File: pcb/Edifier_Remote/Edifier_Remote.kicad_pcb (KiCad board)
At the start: 2 copper layers, 33 x 70 mm, 9 parts, among them Q1 Q_NPN_BCE

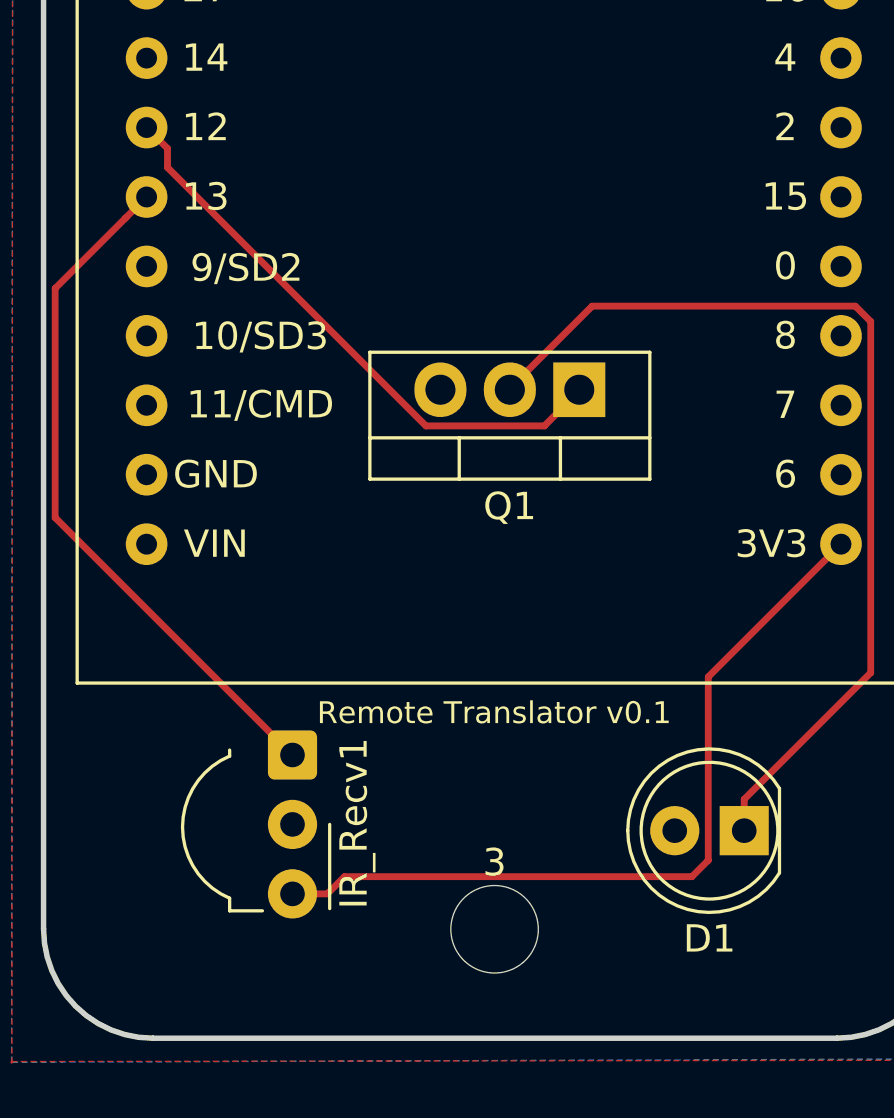
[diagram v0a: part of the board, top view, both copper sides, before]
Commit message: add some labels and rotate Q1
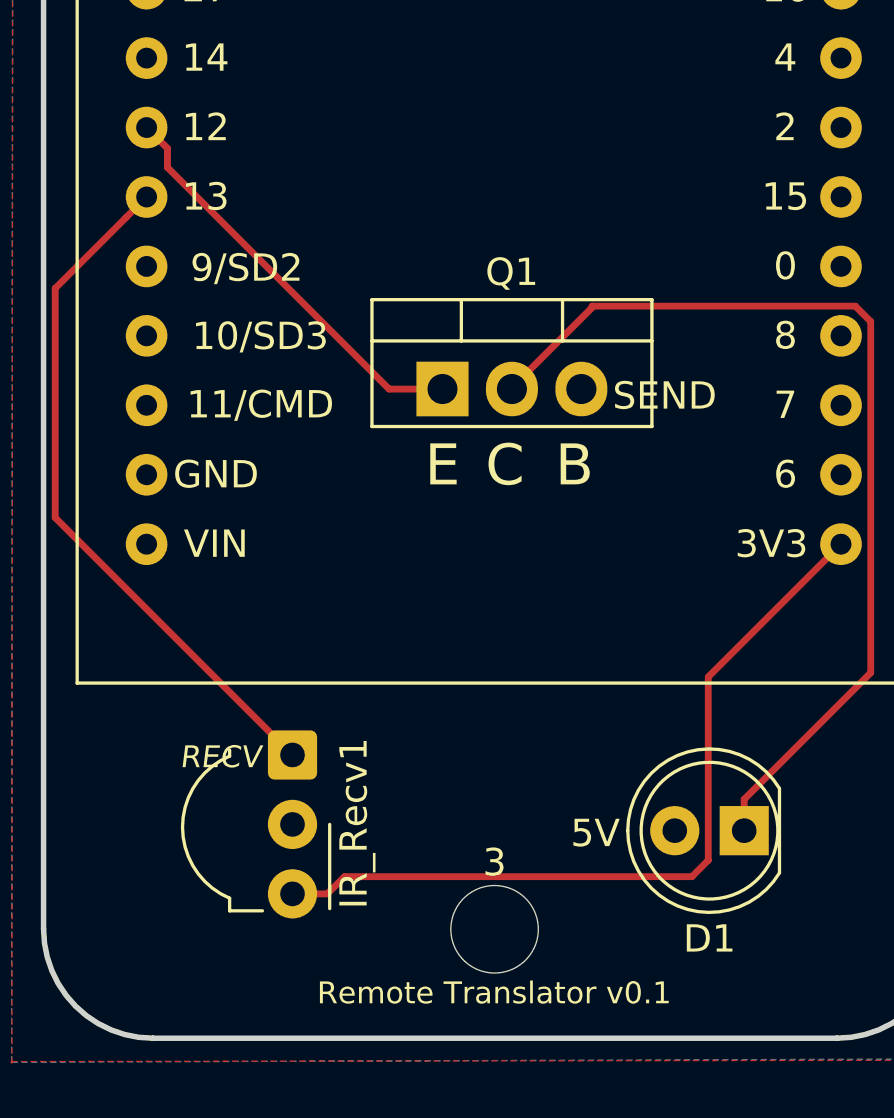
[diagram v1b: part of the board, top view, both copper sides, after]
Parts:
- moved Q1 5.00 mm to (115.6, 112.5), turned to 0 degrees
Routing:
- net /SEND: track 21.3 -> 15.2 mm
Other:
- board text added: "5V"
- board text added: "B"
- board text added: "C"
- board text added: "E"
- board text added: "RECV"
- board text added: "SEND"
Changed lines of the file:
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@@
-(kicad_pcb (version 20171130) (host pcbnew "(5.1.2)-2")
+(kicad_pcb (version 20171130) (host pcbnew 5.0.2)
   (general
     (thickness 1.6)
-    (drawings 3)
-    (tracks 23)
+    (drawings 9)
+    (tracks 24)
     (zones 0)
     (modules 9)
@@
     (zone_45_only no)
     (trace_min 0.2)
+    (segment_width 0.2)
+    (edge_width 0.1)
     (via_size 0.8)
     (via_drill 0.4)
@@
     (uvia_min_size 0.2)
     (uvia_min_drill 0.1)
-    (edge_width 0.1)
-    (segment_width 0.2)
     (pcb_text_width 0.3)
     (pcb_text_size 1.5 1.5)
@@
     (pad_drill 0.762)
     (pad_to_mask_clearance 0)
+    (solder_mask_min_width 0.25)
     (aux_axis_origin 0 0)
     (visible_elements 7FFFFFFF)
@@
       (outputformat 1)
       (mirror false)
-      (drillshape 1)
+      (drillshape 0)
       (scaleselection 1)
-      (outputdirectory ""))
+      (outputdirectory "../Gerber/"))
   )
   (net 0 "")
@@
   )
   (module Package_TO_SOT_THT:TO-220-3_Vertical (layer F.Cu)
-    (at 120.5738 112.5474 180)
+    (at 115.57 112.522)
     (descr "TO-220-3, Vertical, RM 2.54mm, see https://www.vishay.com/docs/66542/to-220-1.pdf")
     (tags "TO-220-3 Vertical RM 2.54mm")
-    (fp_text reference Q1 (at 2.54 -4.27) (layer F.SilkS)
-      (effects (font (size 1 1) (thickness 0.15)))
-    )
-    (fp_text value Q_NPN_BCE (at 2.54 2.5) (layer F.Fab)
-      (effects (font (size 1 1) (thickness 0.15)))
-    )
-    (fp_text user %R (at 2.54 -4.27) (layer F.Fab)
+    (fp_text reference Q1 (at 2.54 -4.27 -180) (layer F.SilkS)
+      (effects (font (size 1 1) (thickness 0.15)))
+    )
+    (fp_text value Q_NPN_BCE (at 1.9558 -2.5146 -180) (layer F.Fab)
+      (effects (font (size 1 1) (thickness 0.15)))
+    )
+    (fp_text user %R (at 2.54 -4.27 -180) (layer F.Fab)
       (effects (font (size 1 1) (thickness 0.15)))
     )
@@
     (fp_line (start -2.46 1.25) (end 7.54 1.25) (layer F.Fab) (width 0.1))
     (fp_line (start -2.46 -3.15) (end -2.46 1.25) (layer F.Fab) (width 0.1))
-    (pad 3 thru_hole oval (at 5.08 0 180) (size 1.905 2) (drill 1.1) (layers *.Cu *.Mask)
+    (pad 3 thru_hole oval (at 5.08 0) (size 1.905 2) (drill 1.1) (layers *.Cu *.Mask)
       (net 4 GND))
-    (pad 2 thru_hole oval (at 2.54 0 180) (size 1.905 2) (drill 1.1) (layers *.Cu *.Mask)
+    (pad 2 thru_hole oval (at 2.54 0) (size 1.905 2) (drill 1.1) (layers *.Cu *.Mask)
       (net 2 "Net-(D1-Pad1)"))
-    (pad 1 thru_hole rect (at 0 0 180) (size 1.905 2) (drill 1.1) (layers *.Cu *.Mask)
+    (pad 1 thru_hole rect (at 0 0) (size 1.905 2) (drill 1.1) (layers *.Cu *.Mask)
       (net 6 /SEND))
     (model ${KISYS3DMOD}/Package_TO_SOT_THT.3dshapes/TO-220-3_Vertical.wrl
@@
     )
   )
+  (gr_text E (at 115.57 115.316) (layer F.SilkS)
+    (effects (font (size 1.5 1.5) (thickness 0.3)))
+  )
+  (gr_text C (at 117.856 115.316) (layer F.SilkS)
+    (effects (font (size 1.5 1.5) (thickness 0.3)))
+  )
+  (gr_text B (at 120.396 115.316) (layer F.SilkS)
+    (effects (font (size 1.5 1.5) (thickness 0.3)))
+  )
+  (gr_text SEND (at 123.698 112.776) (layer F.SilkS)
+    (effects (font (size 1 1) (thickness 0.25)))
+  )
+  (gr_text RECV (at 107.442 125.984) (layer F.SilkS)
+    (effects (font (size 0.8 0.8) (thickness 0.2) italic))
+  )
+  (gr_text 5V (at 121.158 128.778) (layer F.SilkS)
+    (effects (font (size 1 1) (thickness 0.25)))
+  )
   (gr_text "Remote Translator v0.1" (at 117.6782 89.5096) (layer B.SilkS)
     (effects (font (size 1 1) (thickness 0.15)) (justify mirror))
@@
     (effects (font (size 1 1) (thickness 0.15)) (justify mirror))
   )
-  (gr_text "Remote Translator v0.1\n" (at 117.4623 124.3711) (layer F.SilkS)
+  (gr_text "Remote Translator v0.1\n" (at 117.4623 134.62) (layer F.SilkS)
     (effects (font (size 0.8 0.8) (thickness 0.15)))
   )
-  (segment (start 118.0338 112.4999) (end 118.0338 112.5474) (width 0.25) (layer F.Cu) (net 2))
-  (segment (start 121.043701 109.489999) (end 118.0338 112.4999) (width 0.25) (layer F.Cu) (net 2))
   (segment (start 131.234001 110.055239) (end 130.668761 109.489999) (width 0.25) (layer F.Cu) (net 2))
   (segment (start 131.234001 122.898699) (end 131.234001 110.055239) (width 0.25) (layer F.Cu) (net 2))
@@
   (segment (start 126.6063 127.5264) (end 131.234001 122.898699) (width 0.25) (layer F.Cu) (net 2))
   (segment (start 126.6063 128.6764) (end 126.6063 127.5264) (width 0.25) (layer F.Cu) (net 2))
+  (segment (start 118.0338 112.4999) (end 118.0338 112.5474) (width 0.25) (layer F.Cu) (net 2))
+  (segment (start 118.11 112.4745) (end 118.11 112.522) (width 0.25) (layer F.Cu) (net 2))
+  (segment (start 121.043701 109.540799) (end 118.11 112.4745) (width 0.25) (layer F.Cu) (net 2))
+  (segment (start 121.043701 109.489999) (end 121.043701 109.540799) (width 0.25) (layer F.Cu) (net 2))
   (segment (start 111.985993 130.358199) (end 124.693999 130.358199) (width 0.25) (layer F.Cu) (net 3))
   (segment (start 110.0836 130.9878) (end 111.356392 130.9878) (width 0.25) (layer F.Cu) (net 3))
@@
   (segment (start 105.508999 103.718999) (end 104.747 102.957) (width 0.25) (layer F.Cu) (net 6))
   (segment (start 105.508999 104.41677) (end 105.508999 103.718999) (width 0.25) (layer F.Cu) (net 6))
-  (segment (start 114.964639 113.87241) (end 105.508999 104.41677) (width 0.25) (layer F.Cu) (net 6))
-  (segment (start 119.29629 113.87241) (end 114.964639 113.87241) (width 0.25) (layer F.Cu) (net 6))
-  (segment (start 120.5738 112.5949) (end 119.29629 113.87241) (width 0.25) (layer F.Cu) (net 6))
-  (segment (start 120.5738 112.5474) (end 120.5738 112.5949) (width 0.25) (layer F.Cu) (net 6))
+  (segment (start 120.5738 112.5474) (end 120.5738 112.5949) (width 0.25) (layer F.Cu) (net 4))
+  (segment (start 113.614229 112.522) (end 115.57 112.522) (width 0.25) (layer F.Cu) (net 6))
+  (segment (start 105.508999 104.41677) (end 113.614229 112.522) (width 0.25) (layer F.Cu) (net 6))
   (zone (net 4) (net_name GND) (layer F.Cu) (hatch edge 0.508)
     (connect_pads (clearance 0.508))

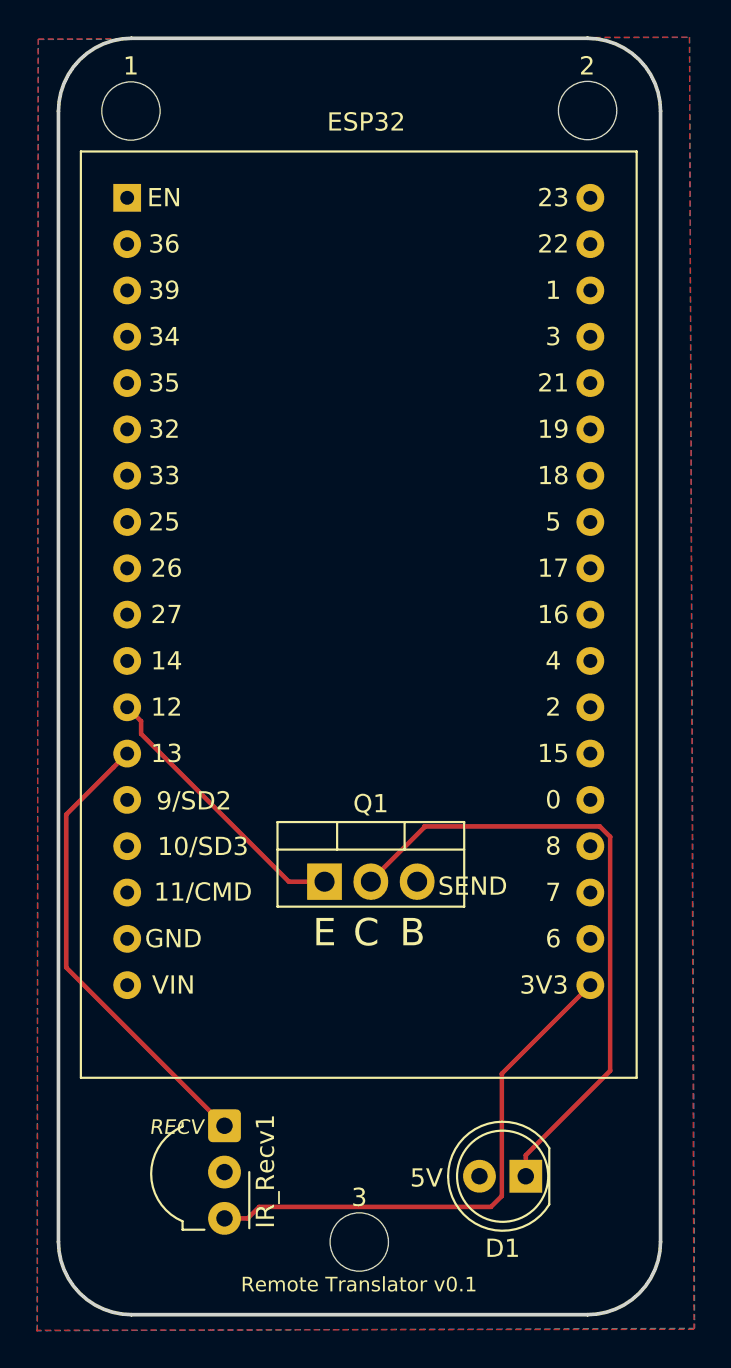
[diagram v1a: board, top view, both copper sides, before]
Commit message: swap ir led and receiver
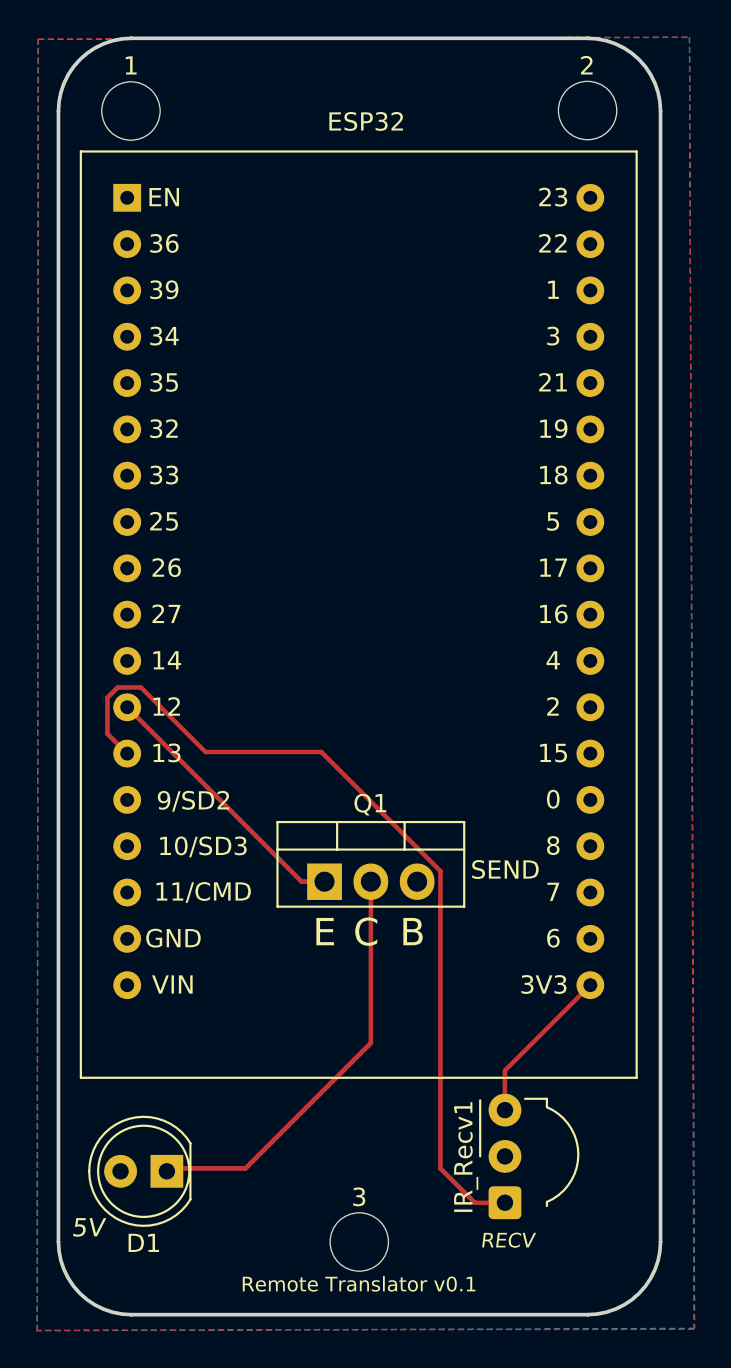
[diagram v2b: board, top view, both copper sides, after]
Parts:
- moved D1 19.7 mm to (106.9, 128.4)
- moved IR_Recv1 16.0 mm to (125.5, 130.1), turned to 90 degrees
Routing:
- net /RECV: track 25.4 -> 46.8 mm
- net /3V3: track 29.3 -> 8.95 mm
- net Net-(D1-Pad1): track 35.3 -> 23.0 mm
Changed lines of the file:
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@@
-(kicad_pcb (version 20171130) (host pcbnew 5.0.2)
+(kicad_pcb (version 20171130) (host pcbnew "(5.1.2)-2")
   (general
     (thickness 1.6)
@@
   (page A4)
   (layers
-    (0 F.Cu signal)
-    (31 B.Cu signal)
+    (0 F.Cu signal hide)
+    (31 B.Cu signal hide)
     (32 B.Adhes user)
     (33 F.Adhes user)
@@
     (zone_45_only no)
     (trace_min 0.2)
-    (segment_width 0.2)
-    (edge_width 0.1)
     (via_size 0.8)
     (via_drill 0.4)
@@
     (uvia_min_size 0.2)
     (uvia_min_drill 0.1)
+    (edge_width 0.1)
+    (segment_width 0.2)
     (pcb_text_width 0.3)
     (pcb_text_size 1.5 1.5)
@@
   )
   (module OptoDevice:Vishay_MOLD-3Pin (layer F.Cu)
-    (at 110.0836 125.9078 270)
+    (at 125.46584 130.12928 90)
     (descr "IR Receiver Vishay TSOP-xxxx, MOLD package, see https://www.vishay.com/docs/82669/tsop32s40f.pdf")
     (tags "IR Receiver Vishay TSOP-xxxx MOLD")
@@
       (effects (font (size 1 1) (thickness 0.15)))
     )
-    (pad 3 thru_hole circle (at 5.08 0 270) (size 1.8 1.8) (drill 0.9) (layers *.Cu *.Mask)
+    (pad 3 thru_hole circle (at 5.08 0 90) (size 1.8 1.8) (drill 0.9) (layers *.Cu *.Mask)
       (net 3 /3V3))
-    (pad 2 thru_hole circle (at 2.54 0 270) (size 1.8 1.8) (drill 0.9) (layers *.Cu *.Mask)
+    (pad 2 thru_hole circle (at 2.54 0 90) (size 1.8 1.8) (drill 0.9) (layers *.Cu *.Mask)
       (net 4 GND))
-    (pad 1 thru_hole roundrect (at 0 0 270) (size 1.8 1.8) (drill 0.9) (layers *.Cu *.Mask) (roundrect_rratio 0.138)
+    (pad 1 thru_hole roundrect (at 0 0 90) (size 1.8 1.8) (drill 0.9) (layers *.Cu *.Mask) (roundrect_rratio 0.138)
       (net 5 /RECV))
     (model ${KISYS3DMOD}/OptoDevice.3dshapes/Vishay_MOLD-3Pin.wrl
@@
   )
   (module LED_THT:LED_D5.0mm (layer F.Cu)
-    (at 126.6063 128.6764 180)
+    (at 106.92384 128.40716 180)
     (descr "LED, diameter 5.0mm, 2 pins, http://cdn-reichelt.de/documents/datenblatt/A500/LL-504BC2E-009.pdf")
     (tags "LED diameter 5.0mm 2 pins")
@@
     (effects (font (size 1.5 1.5) (thickness 0.3)))
   )
-  (gr_text SEND (at 123.698 112.776) (layer F.SilkS)
+  (gr_text SEND (at 125.48616 111.89208) (layer F.SilkS)
     (effects (font (size 1 1) (thickness 0.25)))
   )
-  (gr_text RECV (at 107.442 125.984) (layer F.SilkS)
+  (gr_text RECV (at 125.59284 132.21208) (layer F.SilkS)
     (effects (font (size 0.8 0.8) (thickness 0.2) italic))
   )
-  (gr_text 5V (at 121.158 128.778) (layer F.SilkS)
-    (effects (font (size 1 1) (thickness 0.25)))
+  (gr_text 5V (at 102.58044 131.51104) (layer F.SilkS)
+    (effects (font (size 1 1) (thickness 0.25) italic))
   )
   (gr_text "Remote Translator v0.1" (at 117.6782 89.5096) (layer B.SilkS)
@@
     (effects (font (size 0.8 0.8) (thickness 0.15)))
   )
-  (segment (start 131.234001 110.055239) (end 130.668761 109.489999) (width 0.25) (layer F.Cu) (net 2))
-  (segment (start 131.234001 122.898699) (end 131.234001 110.055239) (width 0.25) (layer F.Cu) (net 2))
-  (segment (start 130.668761 109.489999) (end 121.043701 109.489999) (width 0.25) (layer F.Cu) (net 2))
-  (segment (start 126.6063 127.5264) (end 131.234001 122.898699) (width 0.25) (layer F.Cu) (net 2))
-  (segment (start 126.6063 128.6764) (end 126.6063 127.5264) (width 0.25) (layer F.Cu) (net 2))
   (segment (start 118.0338 112.4999) (end 118.0338 112.5474) (width 0.25) (layer F.Cu) (net 2))
   (segment (start 118.11 112.4745) (end 118.11 112.522) (width 0.25) (layer F.Cu) (net 2))
-  (segment (start 121.043701 109.540799) (end 118.11 112.4745) (width 0.25) (layer F.Cu) (net 2))
-  (segment (start 121.043701 109.489999) (end 121.043701 109.540799) (width 0.25) (layer F.Cu) (net 2))
-  (segment (start 111.985993 130.358199) (end 124.693999 130.358199) (width 0.25) (layer F.Cu) (net 3))
-  (segment (start 110.0836 130.9878) (end 111.356392 130.9878) (width 0.25) (layer F.Cu) (net 3))
-  (segment (start 111.356392 130.9878) (end 111.985993 130.358199) (width 0.25) (layer F.Cu) (net 3))
-  (segment (start 125.291301 129.760897) (end 124.693999 130.358199) (width 0.25) (layer F.Cu) (net 3))
-  (segment (start 125.291301 123.052699) (end 125.291301 129.760897) (width 0.25) (layer F.Cu) (net 3))
-  (segment (start 130.147 118.197) (end 125.291301 123.052699) (width 0.25) (layer F.Cu) (net 3))
-  (segment (start 103.985001 106.258999) (end 104.747 105.497) (width 0.25) (layer F.Cu) (net 5))
-  (segment (start 101.40221 108.84179) (end 103.985001 106.258999) (width 0.25) (layer F.Cu) (net 5))
-  (segment (start 101.40221 117.22641) (end 101.40221 108.84179) (width 0.25) (layer F.Cu) (net 5))
-  (segment (start 110.0836 125.9078) (end 101.40221 117.22641) (width 0.25) (layer F.Cu) (net 5))
-  (segment (start 105.508999 103.718999) (end 104.747 102.957) (width 0.25) (layer F.Cu) (net 6))
-  (segment (start 105.508999 104.41677) (end 105.508999 103.718999) (width 0.25) (layer F.Cu) (net 6))
+  (segment (start 106.985959 128.34504) (end 106.994643 128.357398) (width 0.25) (layer F.Cu) (net 2))
+  (segment (start 107.0864 128.2446) (end 106.985959 128.34504) (width 0.25) (layer F.Cu) (net 2))
+  (segment (start 111.2336 128.2446) (end 107.0864 128.2446) (width 0.25) (layer F.Cu) (net 2))
+  (segment (start 118.11 121.3682) (end 111.2336 128.2446) (width 0.25) (layer F.Cu) (net 2))
+  (segment (start 118.11 112.522) (end 118.11 121.3682) (width 0.25) (layer F.Cu) (net 2))
+  (segment (start 130.147 118.3539) (end 130.147 118.197) (width 0.25) (layer F.Cu) (net 3))
+  (segment (start 125.46584 122.87816) (end 125.46584 125.04928) (width 0.25) (layer F.Cu) (net 3))
+  (segment (start 130.147 118.197) (end 125.46584 122.87816) (width 0.25) (layer F.Cu) (net 3))
   (segment (start 120.5738 112.5474) (end 120.5738 112.5949) (width 0.25) (layer F.Cu) (net 4))
-  (segment (start 113.614229 112.522) (end 115.57 112.522) (width 0.25) (layer F.Cu) (net 6))
-  (segment (start 105.508999 104.41677) (end 113.614229 112.522) (width 0.25) (layer F.Cu) (net 6))
+  (segment (start 103.985001 104.735001) (end 104.747 105.497) (width 0.25) (layer F.Cu) (net 5))
+  (segment (start 103.659999 104.409999) (end 103.985001 104.735001) (width 0.25) (layer F.Cu) (net 5))
+  (segment (start 103.659999 102.435239) (end 103.659999 104.409999) (width 0.25) (layer F.Cu) (net 5))
+  (segment (start 105.502199 101.869999) (end 104.225239 101.869999) (width 0.25) (layer F.Cu) (net 5))
+  (segment (start 121.92751 128.25211) (end 121.92751 111.945339) (width 0.25) (layer F.Cu) (net 5))
+  (segment (start 104.225239 101.869999) (end 103.659999 102.435239) (width 0.25) (layer F.Cu) (net 5))
+  (segment (start 123.80468 130.12928) (end 121.92751 128.25211) (width 0.25) (layer F.Cu) (net 5))
+  (segment (start 121.92751 111.945339) (end 115.392171 105.41) (width 0.25) (layer F.Cu) (net 5))
+  (segment (start 115.392171 105.41) (end 109.0422 105.41) (width 0.25) (layer F.Cu) (net 5))
+  (segment (start 125.46584 130.12928) (end 123.80468 130.12928) (width 0.25) (layer F.Cu) (net 5))
+  (segment (start 109.0422 105.41) (end 105.502199 101.869999) (width 0.25) (layer F.Cu) (net 5))
+  (segment (start 114.312 112.522) (end 104.747 102.957) (width 0.25) (layer F.Cu) (net 6))
+  (segment (start 115.57 112.522) (end 114.312 112.522) (width 0.25) (layer F.Cu) (net 6))
   (zone (net 4) (net_name GND) (layer F.Cu) (hatch edge 0.508)
     (connect_pads (clearance 0.508))
